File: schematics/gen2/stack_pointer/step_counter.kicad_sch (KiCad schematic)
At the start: 16 parts, among them J1 Bus_PCI_Express_x16, U1 74LS00, U2 74LS193, U3 74LS193, U4 74LS193, U5 74LS193, U6 74LS245, U7 74LS245

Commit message: (feat) step_counter update.
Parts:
- removed J1: Bus_PCI_Express_x16, Connector_PCBEdge:BUS_PCIexpress_x16, symbol Connector:Bus_PCI_Express_x16
- added BC1: BusConnector, Connector_PCBEdge:BUS_PCIexpress_x16, symbol cpu816symbols:BusConnector
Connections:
- net BUS0: now also BC1.A51 (DATA0)
- net BUS1: now also BC1.A52 (DATA1)
- net BUS2: now also BC1.A53 (DATA2)
- net BUS3: now also BC1.A54 (DATA3)
- net BUS4: now also BC1.A55 (DATA4)
- net BUS5: now also BC1.A56 (DATA5)
- net BUS6: now also BC1.A57 (DATA6)
- net BUS7: now also BC1.A58 (DATA7)
- net GND: now also BC1.A12 (GND), BC1.A13 (GND), BC1.A23 (GND), BC1.A32 (GND), BC1.A41 (GND), BC1.A50 (GND), BC1.A59 (GND), BC1.A63 (GND), BC1.A64 (GND), BC1.A65 (GND), BC1.A66 (GND), BC1.A70 (GND), BC1.A71 (GND), BC1.A72 (GND), BC1.A73 (GND), BC1.A74 (GND), BC1.A75 (GND), BC1.A76 (GND), BC1.B12 (GND), BC1.B13 (GND), BC1.B23 (GND), BC1.B32 (GND), BC1.B41 (GND), BC1.B50 (GND), BC1.B59 (GND), BC1.B62 (GND), BC1.B63 (GND), BC1.B64 (GND), BC1.B65 (GND), BC1.B66 (GND), BC1.B67 (GND), BC1.B68 (GND), BC1.B69 (GND), BC1.B70 (GND), BC1.B71 (GND), BC1.B72 (GND), BC1.B75 (GND), BC1.B76 (GND)
- net PULSE: now also BC1.B74 (PULSE)
- net Reset: now also BC1.A69 (RESET)
- net SPDec: now also BC1.B53 (SPDEC)
- net SPHighIn: now also BC1.A15 (LSPH)
- net SPInc: now also BC1.B54 (SPINC)
- net SPLowIn: now also BC1.A16 (LSPL)
- net VCC: now also BC1.A1 (VCC), BC1.A2 (VCC), BC1.A3 (VCC), BC1.A4 (VCC), BC1.A5 (VCC), BC1.B1 (VCC), BC1.B2 (VCC), BC1.B3 (VCC), BC1.B4 (VCC), BC1.B5 (VCC)
- net ~{Clk}: now also BC1.B73 (~{CLK})
- net ~{SPHighOut}: now also BC1.B15 (~{RSPH})
- net ~{SPLowOut}: now also BC1.B16 (~{RSPL})
- no-connect marks 4 -> 77
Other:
- moved on the sheet: C1

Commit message: pc and sp sch
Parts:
- removed U1: 74LS00, Package_DIP:DIP-14_W7.62mm_Socket_LongPads, symbol 74xx:74LS00
- removed U2, U3, U4, U5: 74LS193, Package_DIP:DIP-16_W7.62mm_Socket_LongPads, symbol 74xx:74LS193
- removed U6, U7: 74LS245, Package_DIP:DIP-20_W7.62mm_Socket_LongPads, symbol 74xx:74LS245
- added U1: 74HC00, Package_DIP:DIP-14_W7.62mm_Socket_LongPads, symbol 74xx:74HC00
- added U2, U3, U4, U5: 74HC193, Package_DIP:DIP-16_W7.62mm_Socket_LongPads, symbol 74xx:74HC193
- added U6, U7: 74HC245, Package_DIP:DIP-20_W7.62mm_Socket_LongPads, symbol 74xx:74HC245
- C1, C2, C3, C4, C5, C6, C7, C8: footprint Capacitor_THT:CP_Radial_D4.0mm_P1.50mm -> Capacitor_SMD:C_0805_2012Metric_Pad1.18x1.45mm_HandSolder
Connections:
- net CPd: now also U1.6, U4.4 (DOWN)
- net CPu: now also U1.3, U4.5 (UP)
- net DH0: now also U2.3 (QA), U7.18 (B0)
- net DH1: now also U2.2 (QB), U7.17 (B1)
- net DH2: now also U2.6 (QC), U7.16 (B2)
- net DH3: now also U2.7 (QD), U7.15 (B3)
- net DH4: now also U3.3 (QA), U7.14 (B4)
- net DH5: now also U3.2 (QB), U7.13 (B5)
- net DH6: now also U3.6 (QC), U7.12 (B6)
- net DH7: now also U3.7 (QD), U7.11 (B7)
- net DL0: now also U4.3 (QA), U6.18 (B0)
- net DL1: now also U4.2 (QB), U6.17 (B1)
- net DL2: now also U4.6 (QC), U6.16 (B2)
- net DL3: now also U4.7 (QD), U6.15 (B3)
- net DL4: now also U5.3 (QA), U6.14 (B4)
- net DL5: now also U5.2 (QB), U6.13 (B5)
- net DL6: now also U5.6 (QC), U6.12 (B6)
- net DL7: now also U5.7 (QD), U6.11 (B7)
- net GND: now also U1.7 (GND), U2.8 (GND), U3.8 (GND), U4.8 (GND), U5.8 (GND), U6.1 (A->B), U6.10 (GND), U7.1 (A->B), U7.10 (GND)
- net PULSE: now also U1.10, U1.13
- net Ph: now also U1.8, U2.11 (~{LOAD}), U3.11 (~{LOAD})
- net Pl: now also U1.11, U4.11 (~{LOAD}), U5.11 (~{LOAD})
- net VCC: now also U1.14 (VCC), U2.16 (VCC), U3.16 (VCC), U4.16 (VCC), U5.16 (VCC), U6.20 (VCC), U7.20 (VCC)
- net BUS0 renamed DATA0
- net DATA0: now also U2.15 (A), U4.15 (A), U6.2 (A0), U7.2 (A0)
- net BUS1 renamed DATA1
- net DATA1: now also U2.1 (B), U4.1 (B), U6.3 (A1), U7.3 (A1)
- net BUS2 renamed DATA2
- net DATA2: now also U2.10 (C), U4.10 (C), U6.4 (A2), U7.4 (A2)
- net BUS3 renamed DATA3
- net DATA3: now also U2.9 (D), U4.9 (D), U6.5 (A3), U7.5 (A3)
- net BUS4 renamed DATA4
- net DATA4: now also U3.15 (A), U5.15 (A), U6.6 (A4), U7.6 (A4)
- net BUS5 renamed DATA5
- net DATA5: now also U3.1 (B), U5.1 (B), U6.7 (A5), U7.7 (A5)
- net BUS6 renamed DATA6
- net DATA6: now also U3.10 (C), U5.10 (C), U6.8 (A6), U7.8 (A6)
- net BUS7 renamed DATA7
- net DATA7: now also U3.9 (D), U5.9 (D), U6.9 (A7), U7.9 (A7)
- net Reset renamed RESET
- net RESET: now also U2.14 (CLR), U3.14 (CLR), U4.14 (CLR), U5.14 (CLR)
- net SPDec renamed SPDEC
- net SPDEC: now also U1.4
- net SPHighIn renamed LSPH
- net LSPH: now also U1.9
- net SPInc renamed SPINC
- net SPINC: now also U1.1
- net SPLowIn renamed LSPL
- net LSPL: now also U1.12
- net ~{Clk} renamed ~{CLK}
- net ~{CLK}: now also U1.2, U1.5
- net ~{SPHighOut} renamed ~{RSPH}
- net ~{RSPH}: now also U7.19 (CE)
- net ~{SPLowOut} renamed ~{RSPL}
- net ~{RSPL}: now also U6.19 (CE)
- new net: U2.13 (~{BO}), U3.4 (DOWN)
- new net: U2.12 (~{CO}), U3.5 (UP)
- new net: U2.4 (DOWN), U5.13 (~{BO})
- new net: U2.5 (UP), U5.12 (~{CO})
- new net: U4.12 (~{CO}), U5.5 (UP)
- new net: U4.13 (~{BO}), U5.4 (DOWN)

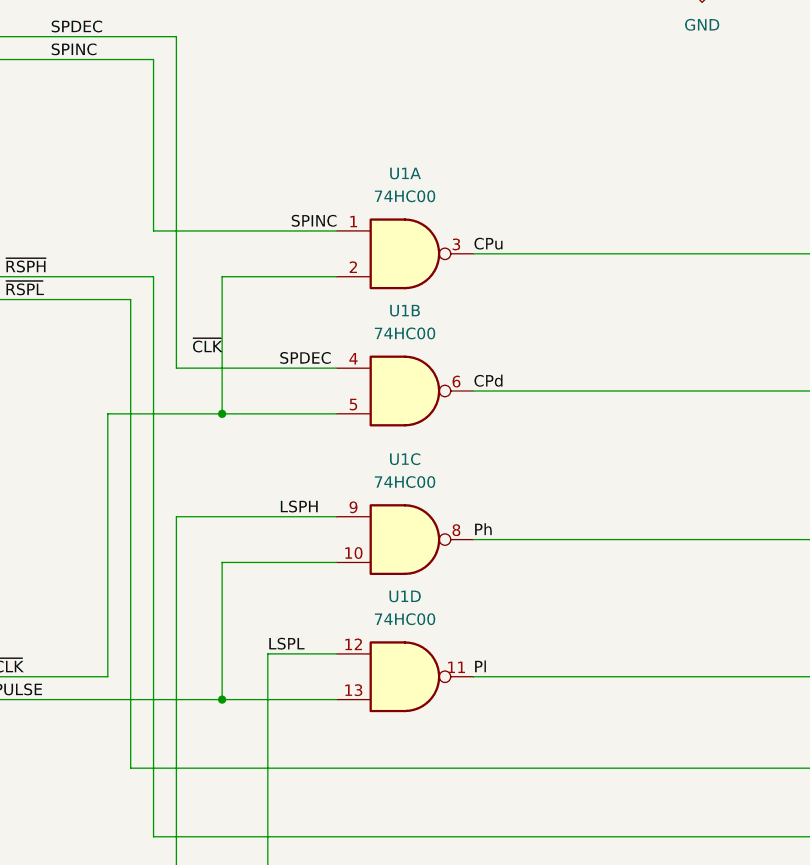
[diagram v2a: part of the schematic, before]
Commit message: (feat) stack pointer and program counter pcb, QA needed.
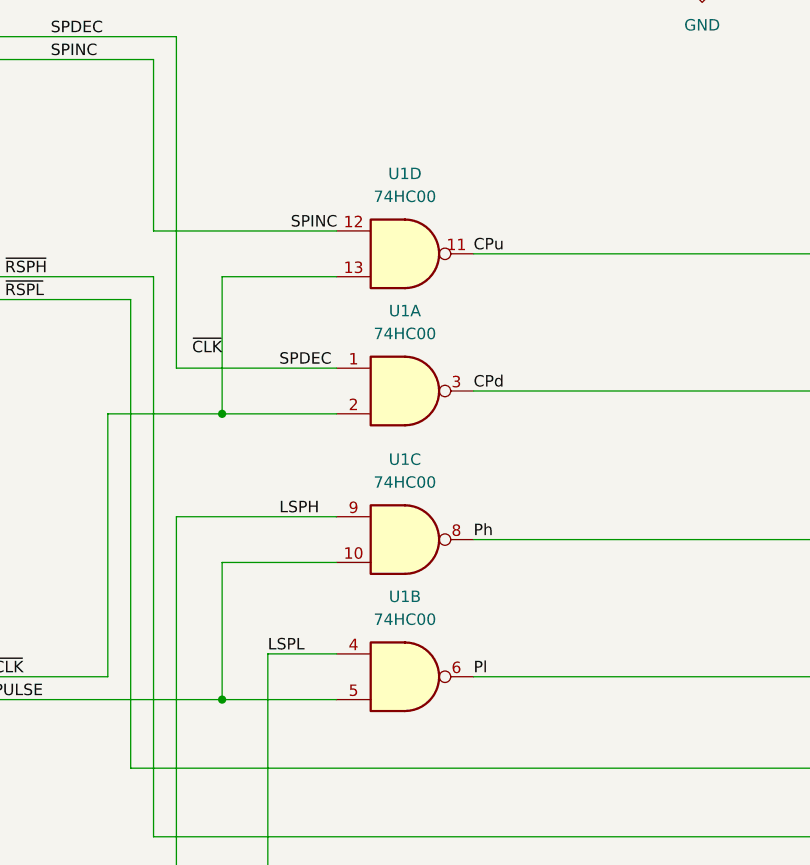
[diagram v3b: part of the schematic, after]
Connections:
- net CPd: now also U1.3; no longer U1.6
- net CPu: now also U1.11; no longer U1.3
- net LSPL: now also U1.4; no longer U1.12
- net PULSE: now also U1.5; no longer U1.13
- net Pl: now also U1.6; no longer U1.11
- net SPDEC: now also U1.1; no longer U1.4
- net SPINC: now also U1.12; no longer U1.1
- net ~{CLK}: now also U1.13; no longer U1.5

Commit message: update
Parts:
- C2, C3, C4, C5, C6, C7, C8: footprint Capacitor_SMD:C_0805_2012Metric_Pad1.18x1.45mm_HandSolder -> Capacitor_THT:C_Disc_D6.0mm_W4.4mm_P5.00mm
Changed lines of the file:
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@@
 			)
 		)
-		(property "Footprint" "Capacitor_SMD:C_0805_2012Metric_Pad1.18x1.45mm_HandSolder"
+		(property "Footprint" "Capacitor_THT:C_Disc_D6.0mm_W4.4mm_P5.00mm"
 			(at 201.93 29.5148 0)
 			(effects
@@
 			)
 		)
-		(property "Footprint" "Capacitor_SMD:C_0805_2012Metric_Pad1.18x1.45mm_HandSolder"
+		(property "Footprint" "Capacitor_THT:C_Disc_D6.0mm_W4.4mm_P5.00mm"
 			(at 283.21 82.8548 0)
 			(effects
@@
 			)
 		)
-		(property "Footprint" "Capacitor_SMD:C_0805_2012Metric_Pad1.18x1.45mm_HandSolder"
+		(property "Footprint" "Capacitor_THT:C_Disc_D6.0mm_W4.4mm_P5.00mm"
 			(at 284.48 166.0652 0)
 			(effects
@@
 			)
 		)
-		(property "Footprint" "Capacitor_SMD:C_0805_2012Metric_Pad1.18x1.45mm_HandSolder"
+		(property "Footprint" "Capacitor_THT:C_Disc_D6.0mm_W4.4mm_P5.00mm"
 			(at 144.78 30.7848 0)
 			(effects
@@
 			)
 		)
-		(property "Footprint" "Capacitor_SMD:C_0805_2012Metric_Pad1.18x1.45mm_HandSolder"
+		(property "Footprint" "Capacitor_THT:C_Disc_D6.0mm_W4.4mm_P5.00mm"
 			(at 341.63 163.5252 0)
 			(effects
@@
 			)
 		)
-		(property "Footprint" "Capacitor_SMD:C_0805_2012Metric_Pad1.18x1.45mm_HandSolder"
+		(property "Footprint" "Capacitor_THT:C_Disc_D6.0mm_W4.4mm_P5.00mm"
 			(at 153.67 112.0648 0)
 			(effects
@@
 			)
 		)
-		(property "Footprint" "Capacitor_SMD:C_0805_2012Metric_Pad1.18x1.45mm_HandSolder"
+		(property "Footprint" "Capacitor_THT:C_Disc_D6.0mm_W4.4mm_P5.00mm"
 			(at 237.49 84.1248 0)
 			(effects

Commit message: complete stack
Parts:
- C1: footprint Capacitor_SMD:C_0805_2012Metric_Pad1.18x1.45mm_HandSolder -> Capacitor_THT:C_Radial_D6.3mm_H5.0mm_P2.50mm
- C2, C3, C4, C5, C6, C7, C8: footprint Capacitor_THT:C_Disc_D6.0mm_W4.4mm_P5.00mm -> Capacitor_THT:C_Disc_D3.0mm_W1.6mm_P2.50mm
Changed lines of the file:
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@@
 			)
 		)
-		(property "Footprint" "Capacitor_THT:C_Disc_D6.0mm_W4.4mm_P5.00mm"
+		(property "Footprint" "Capacitor_THT:C_Disc_D3.0mm_W1.6mm_P2.50mm"
 			(at 201.93 29.5148 0)
 			(effects
@@
 			)
 		)
-		(property "Footprint" "Capacitor_THT:C_Disc_D6.0mm_W4.4mm_P5.00mm"
+		(property "Footprint" "Capacitor_THT:C_Disc_D3.0mm_W1.6mm_P2.50mm"
 			(at 283.21 82.8548 0)
 			(effects
@@
 			)
 		)
-		(property "Footprint" "Capacitor_THT:C_Disc_D6.0mm_W4.4mm_P5.00mm"
+		(property "Footprint" "Capacitor_THT:C_Disc_D3.0mm_W1.6mm_P2.50mm"
 			(at 284.48 166.0652 0)
 			(effects
@@
 			)
 		)
-		(property "Footprint" "Capacitor_SMD:C_0805_2012Metric_Pad1.18x1.45mm_HandSolder"
+		(property "Footprint" "Capacitor_THT:C_Radial_D6.3mm_H5.0mm_P2.50mm"
 			(at 80.01 87.3252 0)
 			(effects
@@
 			)
 		)
-		(property "Footprint" "Capacitor_THT:C_Disc_D6.0mm_W4.4mm_P5.00mm"
+		(property "Footprint" "Capacitor_THT:C_Disc_D3.0mm_W1.6mm_P2.50mm"
 			(at 144.78 30.7848 0)
 			(effects
@@
 			)
 		)
-		(property "Footprint" "Capacitor_THT:C_Disc_D6.0mm_W4.4mm_P5.00mm"
+		(property "Footprint" "Capacitor_THT:C_Disc_D3.0mm_W1.6mm_P2.50mm"
 			(at 341.63 163.5252 0)
 			(effects
@@
 			)
 		)
-		(property "Footprint" "Capacitor_THT:C_Disc_D6.0mm_W4.4mm_P5.00mm"
+		(property "Footprint" "Capacitor_THT:C_Disc_D3.0mm_W1.6mm_P2.50mm"
 			(at 153.67 112.0648 0)
 			(effects
@@
 			)
 		)
-		(property "Footprint" "Capacitor_THT:C_Disc_D6.0mm_W4.4mm_P5.00mm"
+		(property "Footprint" "Capacitor_THT:C_Disc_D3.0mm_W1.6mm_P2.50mm"
 			(at 237.49 84.1248 0)
 			(effects

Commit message: fix(stack pointer): fixed footprints
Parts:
- C2, C3, C4, C5, C6, C7, C8: footprint Capacitor_THT:C_Disc_D3.0mm_W1.6mm_P2.50mm -> Capacitor_THT:C_Disc_D5.0mm_W2.5mm_P5.00mm
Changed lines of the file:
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@@
 			)
 		)
-		(property "Footprint" "Capacitor_THT:C_Disc_D3.0mm_W1.6mm_P2.50mm"
+		(property "Footprint" "Capacitor_THT:C_Disc_D5.0mm_W2.5mm_P5.00mm"
 			(at 201.93 29.5148 0)
 			(effects
@@
 			)
 		)
-		(property "Footprint" "Capacitor_THT:C_Disc_D3.0mm_W1.6mm_P2.50mm"
+		(property "Footprint" "Capacitor_THT:C_Disc_D5.0mm_W2.5mm_P5.00mm"
 			(at 283.21 82.8548 0)
 			(effects
@@
 			)
 		)
-		(property "Footprint" "Capacitor_THT:C_Disc_D3.0mm_W1.6mm_P2.50mm"
+		(property "Footprint" "Capacitor_THT:C_Disc_D5.0mm_W2.5mm_P5.00mm"
 			(at 284.48 166.0652 0)
 			(effects
@@
 			)
 		)
-		(property "Footprint" "Capacitor_THT:C_Disc_D3.0mm_W1.6mm_P2.50mm"
+		(property "Footprint" "Capacitor_THT:C_Disc_D5.0mm_W2.5mm_P5.00mm"
 			(at 144.78 30.7848 0)
 			(effects
@@
 			)
 		)
-		(property "Footprint" "Capacitor_THT:C_Disc_D3.0mm_W1.6mm_P2.50mm"
+		(property "Footprint" "Capacitor_THT:C_Disc_D5.0mm_W2.5mm_P5.00mm"
 			(at 341.63 163.5252 0)
 			(effects
@@
 			)
 		)
-		(property "Footprint" "Capacitor_THT:C_Disc_D3.0mm_W1.6mm_P2.50mm"
+		(property "Footprint" "Capacitor_THT:C_Disc_D5.0mm_W2.5mm_P5.00mm"
 			(at 153.67 112.0648 0)
 			(effects
@@
 			)
 		)
-		(property "Footprint" "Capacitor_THT:C_Disc_D3.0mm_W1.6mm_P2.50mm"
+		(property "Footprint" "Capacitor_THT:C_Disc_D5.0mm_W2.5mm_P5.00mm"
 			(at 237.49 84.1248 0)
 			(effects
